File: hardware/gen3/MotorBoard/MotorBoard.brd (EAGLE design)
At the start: 140 x 107 mm, 198 parts, among them U2 ATMEGA165PV-8AU

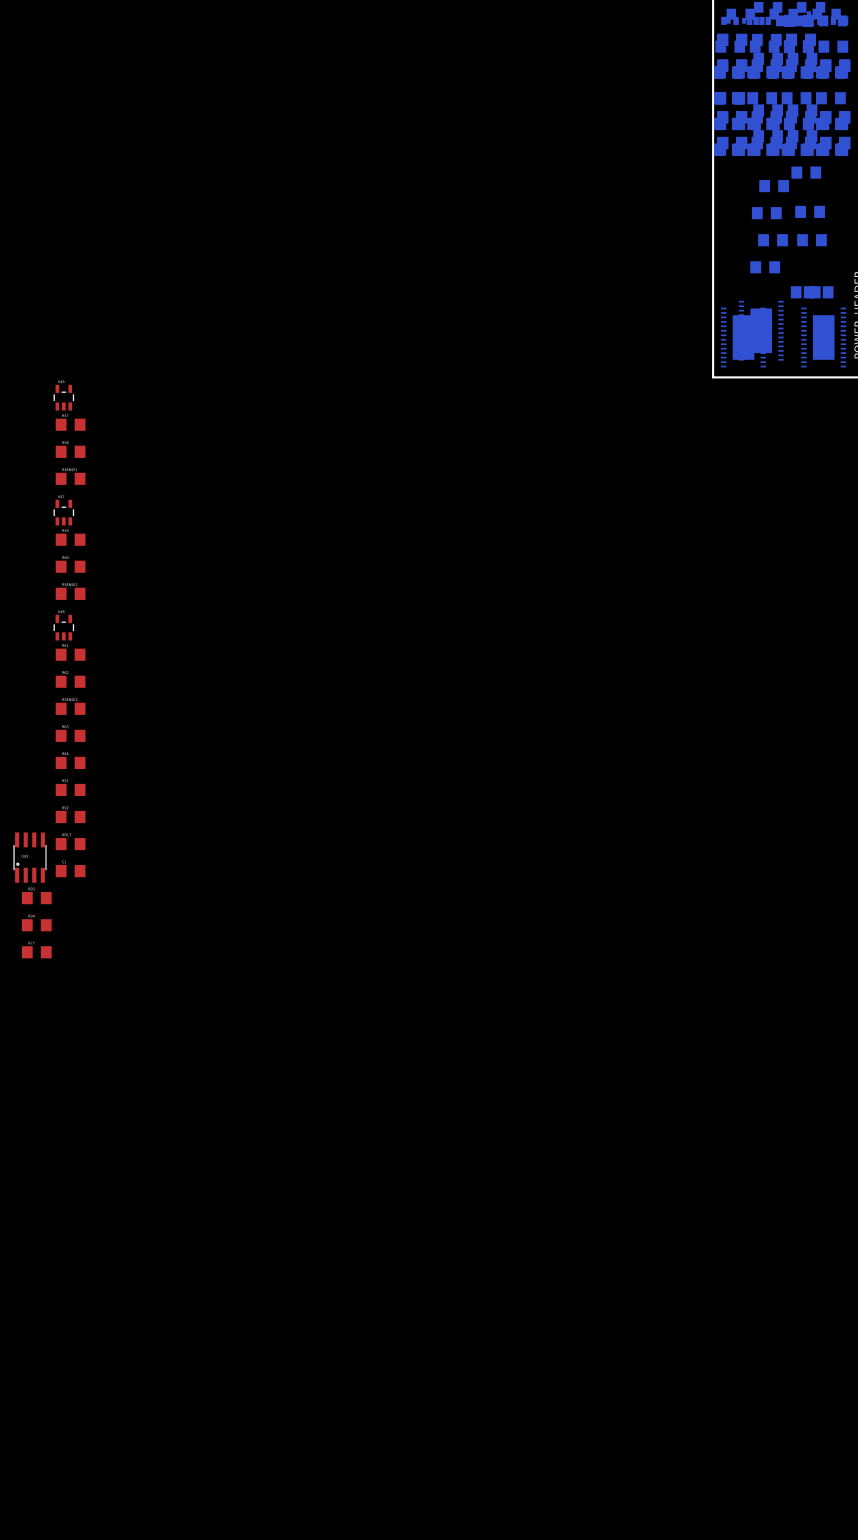
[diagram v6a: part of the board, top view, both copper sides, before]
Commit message: copied to all motors
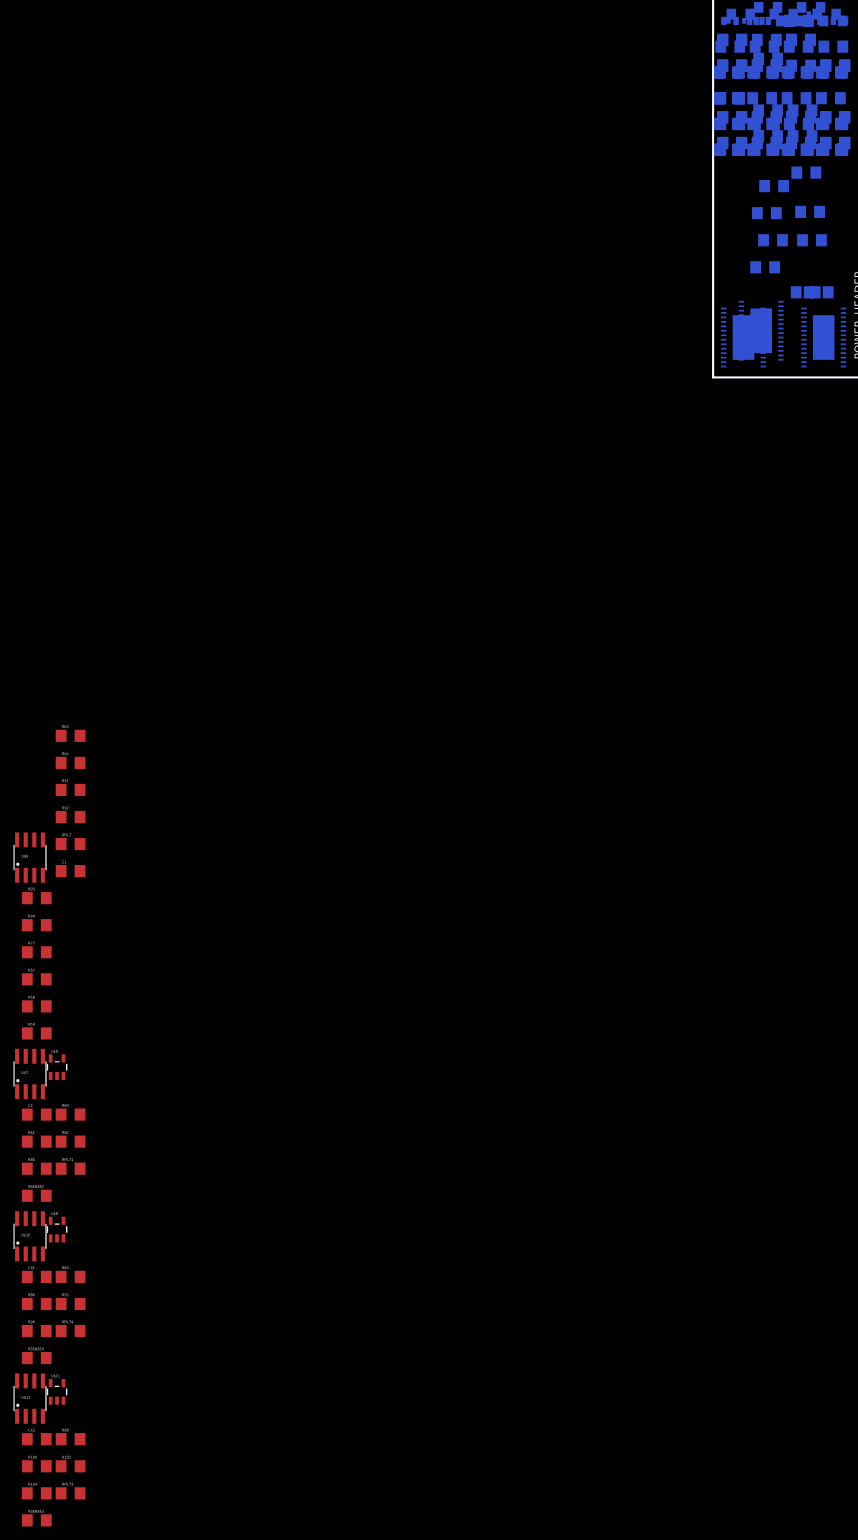
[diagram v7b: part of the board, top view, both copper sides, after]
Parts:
- removed RSENSE: .02, SparkFun-Resistors:1206
- added C2, C41, C42: .1uF, SparkFun-Passives:1206
- added R100: 5k, SparkFun-Resistors:1206
- added R102, R95: 64k, SparkFun-Resistors:1206
- added R104, R96: 36k, SparkFun-Resistors:1206
- added R98: 70k, SparkFun-Resistors:1206
- added RFILT1, RFILT3, RFILT4: 15k, SparkFun-Resistors:1206
- added RSENSE4: .02, SparkFun-Resistors:1206
- added U$10, U$12: LM393, SparkFun-AnalogIC:SO08
- added U$11: MCP6291T-E/OT, SparkFun-AnalogIC:SOT23-5
- R57, R59: value 70k -> 3k
- R58: value 5k -> 3k
- R60: value 5k -> 70k
- R61: value 70k -> 5k
- R62: value 5k -> 64k
- R80: value 1k -> 36k
- R83: value 1k -> 70k
- R86: value 1k -> 5k
- U$7: value MCP6291T-E/OT -> LM393; device SparkFun-AnalogIC:SOT23-5 -> SparkFun-AnalogIC:SO08
- moved R86 217.4 mm to (-100.0, -137.0), flipped to the top
- moved R83 210.1 mm to (-95.0, -133.0), flipped to the top
- moved R80 198.4 mm to (-100.0, -117.0), flipped to the top
- moved RSENSE1 127.2 mm to (12.7, 52.7), flipped to the bottom
- moved RSENSE3 120.1 mm to (-100.0, -169.0)
- moved U$6 99.0 mm to (-97.0, -102.0)
- moved RSENSE2 89.1 mm to (-100.0, -121.0)
- moved U$8 89.0 mm to (-97.0, -126.0)
- moved U$7 83.2 mm to (-101.0, -103.0)
- moved R57 82.2 mm to (-100.0, -89.0)
- moved R58 82.2 mm to (-100.0, -93.0)
- moved R60 81.0 mm to (-95.0, -109.0)
- moved R59 73.2 mm to (-100.0, -97.0)
- moved R61 72.2 mm to (-100.0, -113.0)
- moved R62 68.0 mm to (-95.0, -113.0)
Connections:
- removed net N$100: R80.1, U$1.ENABLE
- removed net N$103: R83.1, U$3.ENABLE
- removed net N$108: R86.1, U$2.ENABLE
- new net LIM2: R57.2, U$1.ENABLE, U$7.1
- new net LIM3: R59.2, U$12.1, U$2.ENABLE
- new net LIM4: R58.2, U$10.1, U$3.ENABLE
- new net N$67: R83.1, R86.2, U$8.4
- new net N$87: C41.1, RFILT4.2, U$8.3
- new net N$88: R95.1, R96.2, U$10.2
- new net N$89: R100.2, R98.1, U$11.4
- new net N$90: C42.1, RFILT3.2, U$11.3
- new net N$91: R102.1, R104.2, U$12.2
- net 12VGND: now also RSENSE4.1; no longer RSENSE.1
- net 5V: now also R102.2, R62.2, R95.2, U$10.8, U$11.5, U$12.8, U$7.8; no longer U$7.5
- net GND: now also C2.2, C41.2, C42.2, R100.1, R104.1, R61.1, R80.1, R86.1, R96.1, U$10.4, U$11.2, U$12.4, U$7.4; no longer R58.1, R60.1, R62.1, U$7.2
- net N$15: now also C2.1, RFILT1.2, U$6.3; no longer R59.1, R60.2, U$7.4
- net N$2: now also R60.1, R61.2; no longer R57.1, R58.2
- net N$22: now also R62.1, R80.2, U$7.2; no longer R61.1, R62.2, U$8.4
- net O1: now also RSENSE1.2; no longer RSENSE.2
- net O2: now also RFILT1.1, RSENSE2.2; no longer RSENSE1.2, U$6.3
- net O3: now also RFILT3.1; no longer U$8.3
- net O4: now also RFILT4.1, RSENSE4.2; no longer RSENSE2.2, U$7.3
- net PWM2: now also R57.1; no longer R80.2
- net PWM3: now also R59.1; no longer R86.2
- net PWM4: now also R58.1; no longer R83.2
- net SENSE2: now also R60.2, U$7.3; no longer R57.2
- net SENSE3: now also R98.2, U$11.1, U$12.3; no longer R61.2, U$8.1
- net SENSE4: now also R83.2, U$10.3, U$8.1; no longer R59.2, U$7.1

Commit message: decoupling
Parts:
- added C43: 100uF, SparkFun-Capacitors:EIA3216
- added C44, C45, C46: .1uF, SparkFun-Passives:1206
- C16, C25, C34, C7: value 1000uF -> 100uF
- C17, C26, C35, C8: value 1000uF -> .1uF; device SparkFun-Capacitors:EIA3216 -> SparkFun-Passives:1206
- moved C35 275.0 mm to (-100.0, -185.0), flipped to the top
- moved C26 259.3 mm to (-100.0, -181.0), flipped to the top
- moved C17 255.8 mm to (-100.0, -177.0), flipped to the top
- moved C8 254.6 mm to (-100.0, -173.0), flipped to the top
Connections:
- net 12V: now also C17.1, C26.1, C35.1, C43.A, C44.1, C8.1; no longer C17.A, C26.A, C35.A, C8.A
- net 12VGND: now also C17.2, C26.2, C35.2, C43.C, C44.2, C8.2; no longer C17.C, C26.C, C35.C, C8.C
- net 3.3V: now also C45.1
- net 5V: now also C46.1
- net GND: now also C45.2, C46.2
